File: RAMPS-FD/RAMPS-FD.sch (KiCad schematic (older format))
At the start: 7 parts, among them M101 LOGO_OSHW, M102 PCB_GREEN_RMC, P106 CONN_3X2, SW101 SW_PUSH

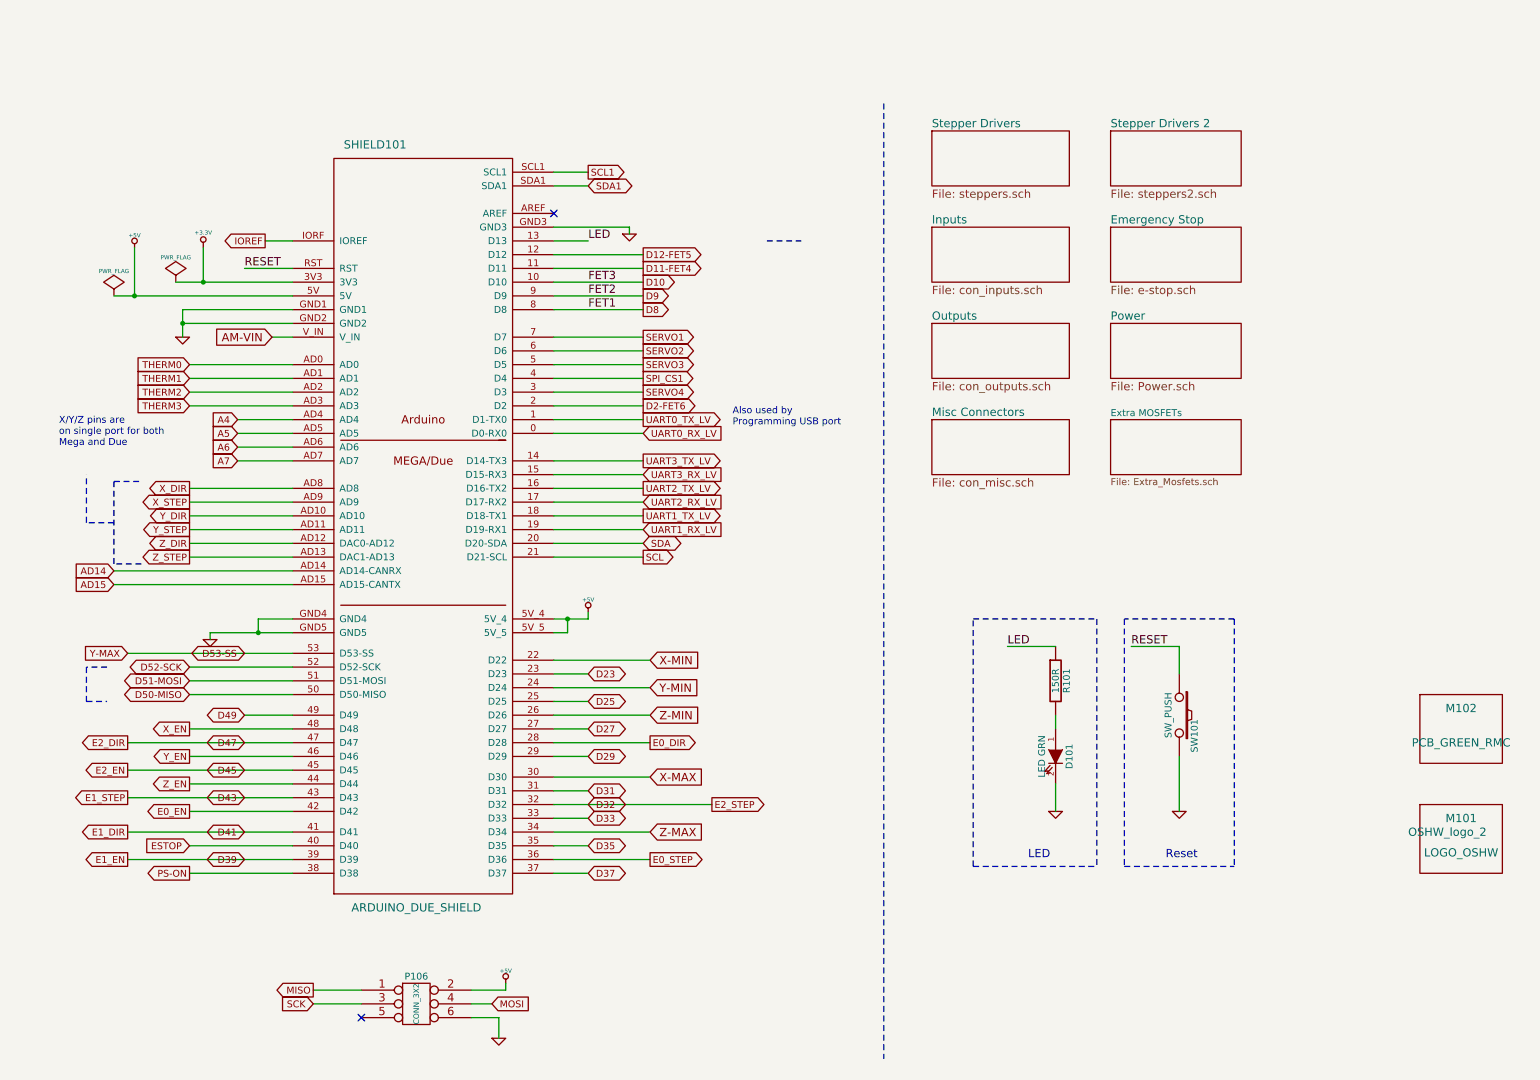
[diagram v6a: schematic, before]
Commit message: RAMPS-FD: update schematic, layout
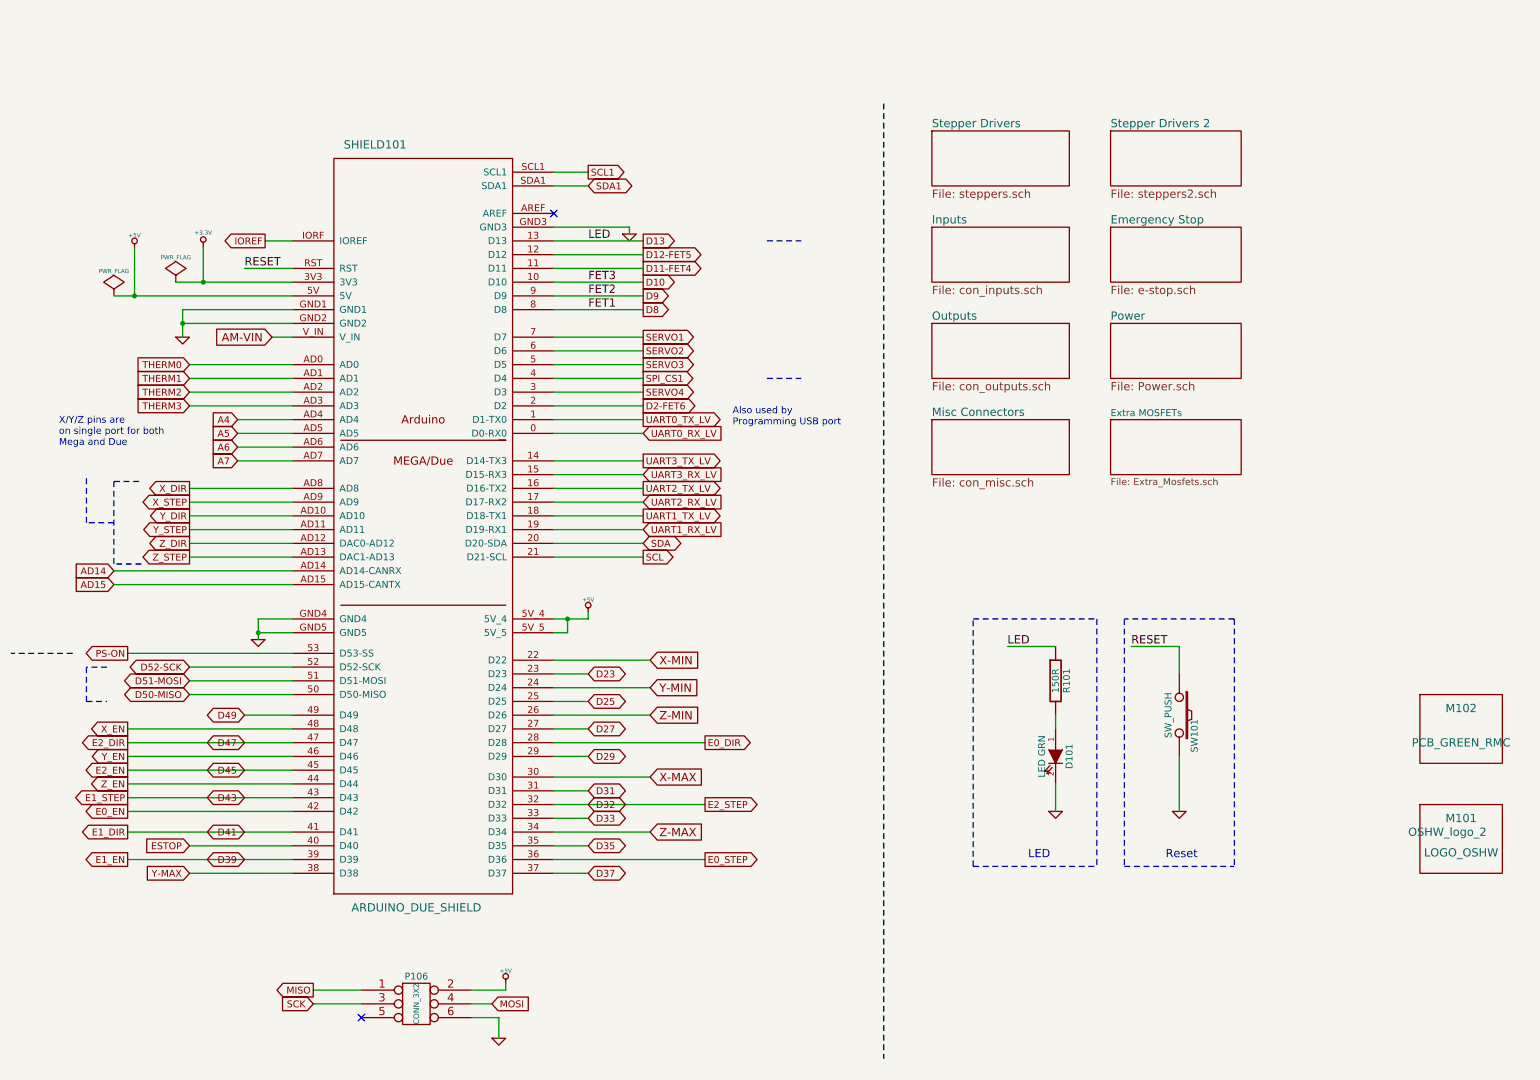
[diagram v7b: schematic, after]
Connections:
- net D53-SS is gone; now on net PS-ON: SHIELD101.53 (D53-SS)
- net PS-ON: no longer SHIELD101.38 (D38)
- net LED renamed D13
- new net Y-MAX: SHIELD101.38 (D38)
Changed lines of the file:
@@
 Sheet 1 9
 Title "RAMPS-FD (RAMPS for Arduino Due)"
-Date "24 sep 2013"
+Date "26 sep 2013"
 Rev "0.2"
 Comp ""
@@
 Text GLabel 1450 4850 0    50   BiDi ~ 0
 D51-MOSI
-Text GLabel 1450 6250 0    50   Output ~ 0
+Text GLabel 1000 4650 0    50   Output ~ 0
 PS-ON
 Text GLabel 1800 3250 0    50   Input ~ 0
@@
 F1 "con_misc.sch" 60
 $EndSheet
-Text GLabel 5250 5750 2    50   Output ~ 0
+Text GLabel 5200 5750 2    50   Output ~ 0
 E2_STEP
 Text GLabel 1000 5300 0    50   Output ~ 0
@@
 Text GLabel 1850 5300 0    50   BiDi ~ 0
 D47
-Text GLabel 1850 4650 0    50   BiDi ~ 0
-D53-SS
 Text GLabel 1850 5100 0    50   BiDi ~ 0
 D49
@@
 Text GLabel 4800 5950 2    60   Input ~ 0
 Z-MAX
-Text GLabel 1000 4650 0    50   Input ~ 0
+Text GLabel 1450 6250 0    50   Input ~ 0
 Y-MAX
 Text GLabel 4800 4900 2    60   Input ~ 0
@@
 Text GLabel 1000 5700 0    50   Output ~ 0
 E1_STEP
-Text GLabel 1450 5200 0    50   Output ~ 0
+Text GLabel 1000 5200 0    50   Output ~ 0
 X_EN
 Text GLabel 1000 5950 0    50   Output ~ 0
@@
 Text GLabel 1000 6150 0    50   Output ~ 0
 E1_EN
-Text GLabel 4800 5300 2    50   Output ~ 0
+Text GLabel 5200 5300 2    50   Output ~ 0
 E0_DIR
-Text GLabel 4800 6150 2    50   Output ~ 0
+Text GLabel 5200 6150 2    50   Output ~ 0
 E0_STEP
-Text GLabel 1450 5800 0    50   Output ~ 0
+Text GLabel 1000 5800 0    50   Output ~ 0
 E0_EN
 Text GLabel 1450 2750 0    50   Input ~ 0
@@
 Text GLabel 1450 2550 0    50   Input ~ 0
 THERM0
-Text GLabel 1450 5600 0    50   Output ~ 0
+Text GLabel 1000 5600 0    50   Output ~ 0
 Z_EN
 Text GLabel 1450 3650 0    50   Output ~ 0
@@
 Text GLabel 1450 3750 0    50   Output ~ 0
 Y_STEP
-Text GLabel 1450 5400 0    50   Output ~ 0
+Text GLabel 1000 5400 0    50   Output ~ 0
 Y_EN
 Text GLabel 1450 3450 0    50   Output ~ 0
@@
 L GND #PWR011
 U 1 1 50FC1A31
-P 1600 4550
-F 0 "#PWR011" H 1600 4550 30  0001 C CNN
-F 1 "GND" H 1600 4480 30  0001 C CNN
-F 2 "" H 1600 4550 60  0001 C CNN
-F 3 "" H 1600 4550 60  0001 C CNN
-	1    1600 4550
+P 1950 4550
+F 0 "#PWR011" H 1950 4550 30  0001 C CNN
+F 1 "GND" H 1950 4480 30  0001 C CNN
+F 2 "" H 1950 4550 60  0001 C CNN
+F 3 "" H 1950 4550 60  0001 C CNN
+	1    1950 4550
 	1    0    0    -1
 $EndComp
@@
 	1450 3850 2200 3850
 Wire Wire Line
-	1450 5800 2200 5800
+	1000 5800 2200 5800
 Connection ~ 1050 2050
 Wire Wire Line
@@
 	9050 4400 8250 4400
 Wire Wire Line
-	1450 5400 2200 5400
+	1000 5400 2200 5400
 Wire Wire Line
 	1350 1950 2200 1950
 Wire Wire Line
-	4100 6150 4800 6150
+	4100 6150 5200 6150
 Wire Wire Line
 	4100 4900 4800 4900
 Wire Wire Line
-	4100 5300 4800 5300
+	4100 5300 5200 5300
 Wire Wire Line
 	4100 5950 4800 5950
@@
 Connection ~ 1950 4500
 Wire Wire Line
-	1950 4500 1950 4400
+	1950 4400 1950 4550
 Wire Wire Line
 	1950 4400 2200 4400
@@
 	4200 4500 4100 4500
 Wire Wire Line
-	1600 4500 2200 4500
-Wire Wire Line
-	1600 4500 1600 4550
+	1950 4500 2200 4500
 Wire Wire Line
 	1050 1700 1050 2050
@@
 Connection ~ 1550 1950
 Wire Wire Line
-	2200 5200 1450 5200
-Wire Wire Line
-	4350 1650 4100 1650
+	2200 5200 1000 5200
+Wire Wire Line
+	4750 1650 4100 1650
 Wire Notes Line
 	7150 6200 8050 6200
@@
 	1800 3050 2200 3050
 Wire Wire Line
-	2200 5600 1450 5600
+	2200 5600 1000 5600
 Wire Wire Line
 	1000 4650 2200 4650
@@
 	4100 5400 4350 5400
 Wire Wire Line
-	4100 5750 5250 5750
+	4100 5750 5200 5750
 Wire Wire Line
 	4350 6050 4100 6050
@@
 Text GLabel 4350 5750 2    50   BiDi ~ 0
 D32
+Wire Notes Line
+	600  4650 150  4650
+Wire Notes Line
+	5650 2650 5900 2650
+Text GLabel 4750 1650 2    50   Output ~ 0
+D13
 $EndSCHEMATC

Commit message: RAMPS-FD: version 1 Rev A
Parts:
- added P102: RESET, symbol CONN_2
- SW101: value SW_PUSH -> RESET
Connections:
- net GND: now also P102.2 (PM)
- net RESET: now also P102.1 (P1)
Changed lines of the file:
@@
 Sheet 1 9
 Title "RAMPS-FD (RAMPS for Arduino Due)"
-Date "26 sep 2013"
+Date "3 oct 2013"
 Rev "0.2"
 Comp ""
@@
 P 8650 5100
 F 0 "SW101" H 8800 5210 50  0000 C CNN
-F 1 "SW_PUSH" H 8650 5020 50  0000 C CNN
+F 1 "RESET" H 8650 5020 50  0000 C CNN
 F 2 "" H 8650 5100 60  0001 C CNN
 F 3 "" H 8650 5100 60  0001 C CNN
@@
 	4750 1850 4100 1850
 Wire Notes Line
-	9050 4400 9050 6200
-Wire Notes Line
-	9050 4400 8250 4400
+	9750 6200 9750 4400
+Wire Notes Line
+	9750 4400 8250 4400
 Wire Wire Line
 	1000 5400 2200 5400
@@
 	8250 4400 8250 6200
 Wire Notes Line
-	8250 6200 9050 6200
+	8250 6200 9750 6200
 Wire Notes Line
 	7150 6200 7150 4400
@@
 	1450 6050 2200 6050
 Wire Wire Line
-	8300 4600 8650 4600
+	8300 4600 9100 4600
 Wire Wire Line
 	8650 4600 8650 4800
@@
 Text GLabel 4750 1650 2    50   Output ~ 0
 D13
+$Comp
+L CONN_2 P102
+U 1 1 52475D81
+P 9500 5100
+F 0 "P102" V 9450 5100 40  0000 C CNN
+F 1 "RESET" V 9550 5100 40  0000 C CNN
+F 2 "" H 9500 5100 60  0000 C CNN
+F 3 "" H 9500 5100 60  0000 C CNN
+	1    9500 5100
+	1    0    0    -1
+$EndComp
+Wire Wire Line
+	9100 4600 9100 5000
+Wire Wire Line
+	9100 5000 9150 5000
+Connection ~ 8650 4600
+Wire Wire Line
+	9150 5200 9150 5700
+Wire Wire Line
+	9150 5700 8650 5700
+Connection ~ 8650 5700
 $EndSCHEMATC
